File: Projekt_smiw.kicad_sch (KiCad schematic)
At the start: 19 parts, among them J1 PWR 5V, J2 JTAG, J3 Conn, SW1 SW_Omron_B3FS, SW2 SW_Omron_B3FS, U1 NCP1117-2.85_TO252, U2 ESP32-S3-PICO-1

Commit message: Orange 21.39
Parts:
- added J7: PWR 5V, symbol Connector_Generic:Conn_01x02
- C6: value ??? -> 10μF
- R2: value 0 -> 10k
- R6: value ??? -> 10k
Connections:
- net BOOT: now also C2.2, SW2.2; no longer R2.2
- net GND: now also J7.2 (Pin_2)
- net ROW 3: now also U2.19 (GPIO14); no longer U2.8 (GPIO3)
- net VDD3: now also R2.1
- new net: J7.1 (Pin_1), R2.2, U2.8 (GPIO3)
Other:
- moved on the sheet: SW2

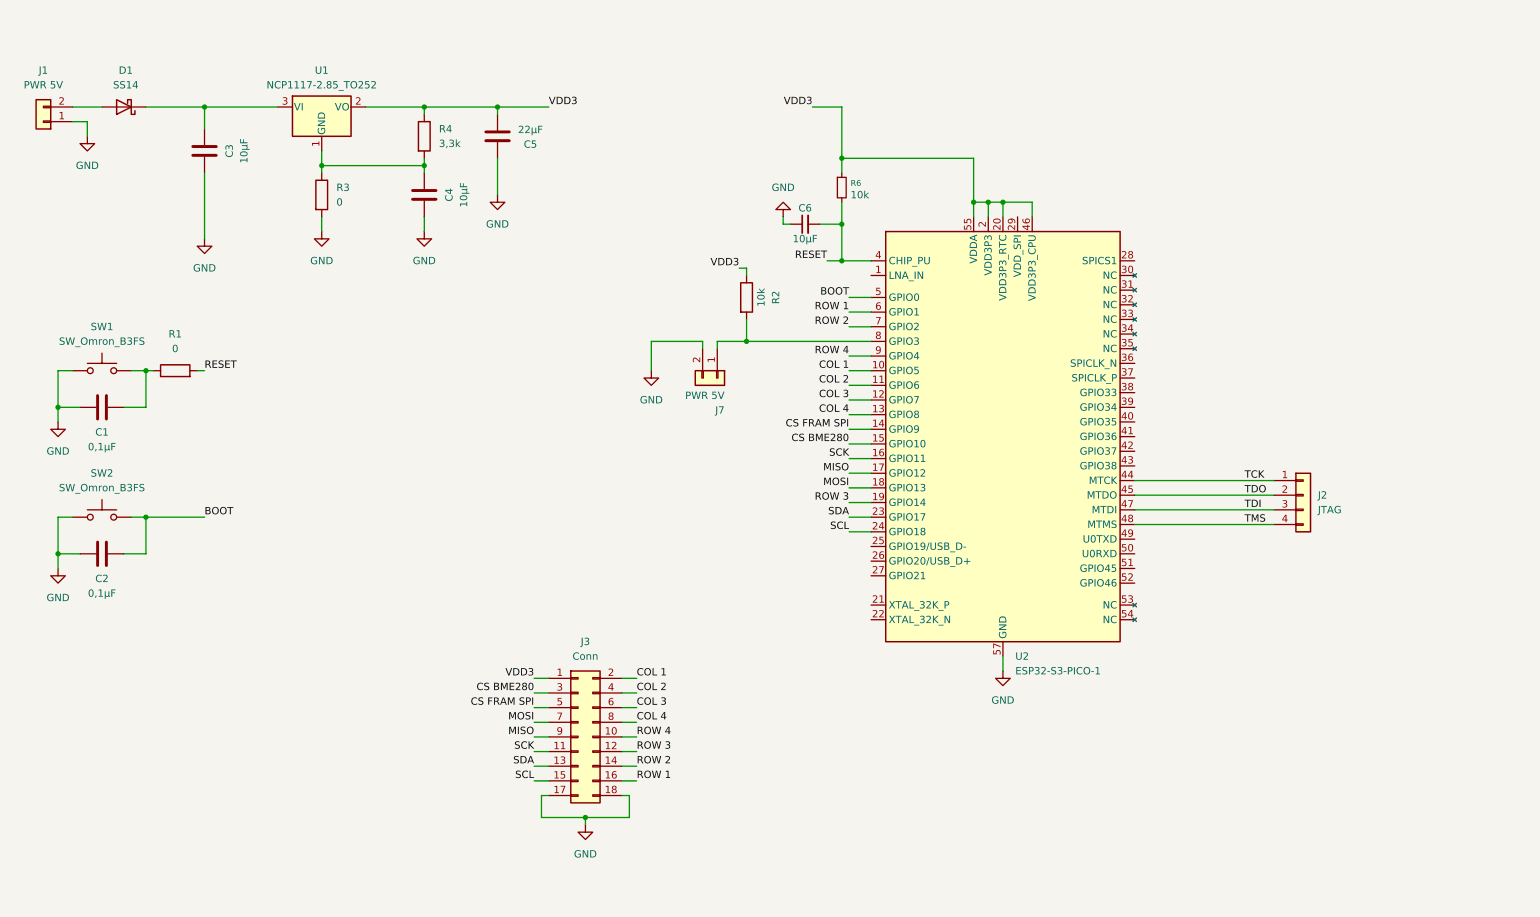
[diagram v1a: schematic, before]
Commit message: USB C update
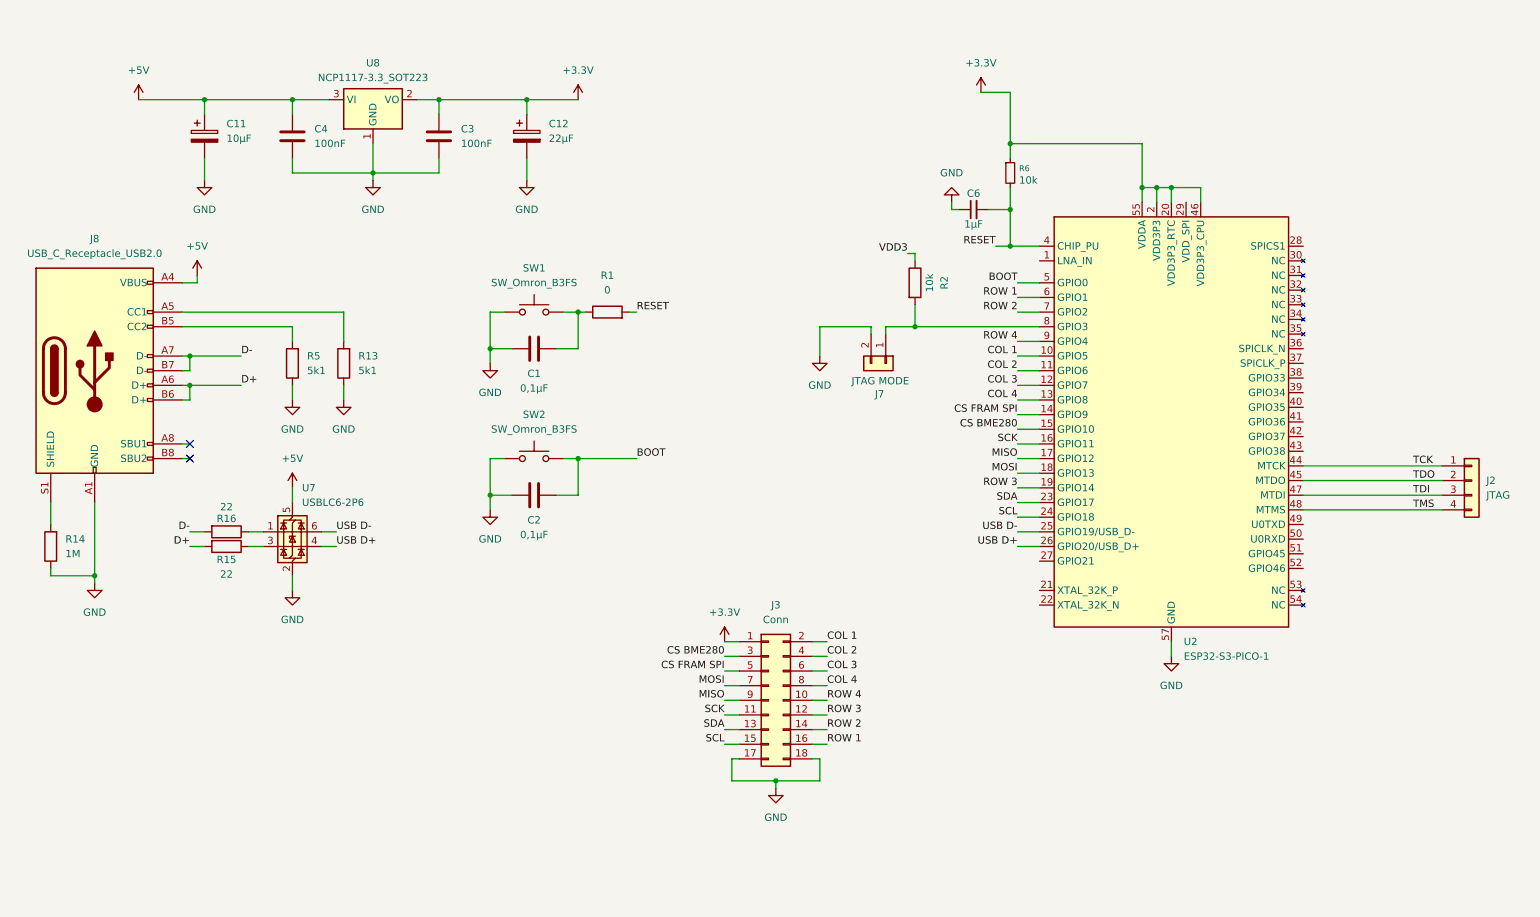
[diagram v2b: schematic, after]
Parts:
- removed C5: 22μF, symbol Device:C
- removed D1: SS14, Diode_SMD:D_SMA, symbol Diode:SS14
- removed J1: PWR 5V, symbol Connector_Generic:Conn_01x02
- removed R3: 0, symbol Device:R
- removed R4: 3,3k, symbol Device:R
- removed U1: NCP1117-2.85_TO252, Package_TO_SOT_SMD:TO-252-2, symbol Regulator_Linear:NCP1117-2.85_TO252
- added C11: 10μF, symbol Device:C_Polarized
- added C12: 22μF, symbol Device:C_Polarized
- added J8: USB_C_Receptacle_USB2.0, symbol Connector:USB_C_Receptacle_USB2.0
- added R13, R5: 5k1, symbol Device:R
- added R14: 1M, symbol Device:R
- added R15, R16: 22, symbol Device:R
- added U7: USBLC6-2P6, Package_TO_SOT_SMD:SOT-666, symbol Power_Protection:USBLC6-2P6
- added U8: NCP1117-3.3_SOT223, Package_TO_SOT_SMD:SOT-223-3_TabPin2, symbol Regulator_Linear:NCP1117-3.3_SOT223
- C3, C4: value 10μF -> 100nF
- C6: value 10μF -> 1μF
- J7: value PWR 5V -> JTAG MODE
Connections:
- net GND: now also C3.2, C4.2, C11.2, C12.2, J8.A1 (GND), J8.A12 (GND), J8.B1 (GND), J8.B12 (GND), R13.1, R14.1, R5.1, U7.2 (GND), U8.1 (GND); no longer C3.1, C4.1
- net VDD3: no longer J3.1 (Pin_1), R6.1, U2.2 (VDD3P3), U2.20 (VDD3P3_RTC), U2.3 (VDD3P3), U2.46 (VDD3P3_CPU), U2.55 (VDDA), U2.56 (VDDA)
- net USB D-: now reaches U2.25 (GPIO19/USB_D-)
- net USB D-: now also U7.6 (I/O1)
- net USB D+: now reaches U2.26 (GPIO20/USB_D+)
- net USB D+: now also U7.4 (I/O2)
- new net: R16.1, U7.1 (I/O1)
- new net: R15.1, U7.3 (I/O2)
- new net: J8.A5 (CC1), R13.2
- new net: J8.B5 (CC2), R5.2
- new net: J8.S1 (SHIELD), R14.2
- new net +3.3V: C12.1, C3.1, J3.1 (Pin_1), R6.1, U2.2 (VDD3P3), U2.20 (VDD3P3_RTC), U2.3 (VDD3P3), U2.46 (VDD3P3_CPU), U2.55 (VDDA), U2.56 (VDDA), U8.2 (VO)
- new net +5V: C11.1, C4.1, J8.A4 (VBUS), J8.A9 (VBUS), J8.B4 (VBUS), J8.B9 (VBUS), U7.5 (VBUS), U8.3 (VI)
- new net D+: J8.A6 (D+), J8.B6 (D+), R15.2
- new net D-: J8.A7 (D-), J8.B7 (D-), R16.2
- no-connect marks 0 -> 2
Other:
- moved on the sheet: C1, C2, C6, J2, J3, J7, R1, R2, R6, SW1, SW2, U2

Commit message: szczerze nie pamiętam co się tutaj zmieniło
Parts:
- removed J7: JTAG MODE, symbol Connector_Generic:Conn_01x02
- removed R14: 1M, symbol Device:R
- removed R15, R16: 22, symbol Device:R
- removed R2: 10k, symbol Device:R
- added R14, R15, R16, R17: 10k, symbol Device:R_Small
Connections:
- net +3.3V: now also R14.1, R15.1, R16.2, R17.2
- net COL 1: now also U2.9 (GPIO4); no longer U2.10 (GPIO5)
- net COL 2: now also U2.10 (GPIO5); no longer U2.11 (GPIO6)
- net COL 3: now also U2.11 (GPIO6); no longer U2.12 (GPIO7)
- net COL 4: now also U2.12 (GPIO7); no longer U2.13 (GPIO8)
- net CS BME280: now also U2.7 (GPIO2), R17.1; no longer U2.15 (GPIO10)
- net CS FRAM SPI: now also U2.6 (GPIO1), R16.1; no longer U2.14 (GPIO9)
- net D+: now also U7.3 (I/O2)
- net D-: now also U7.1 (I/O1)
- net GND: now also J8.S1 (SHIELD)
- net MISO: now also U2.18 (GPIO13); no longer U2.17 (GPIO12)
- net MOSI: now also U2.19 (GPIO14); no longer U2.18 (GPIO13)
- net ROW 1: now also U2.13 (GPIO8); no longer U2.6 (GPIO1)
- net ROW 2: now also U2.14 (GPIO9); no longer U2.7 (GPIO2)
- net ROW 3: now also U2.15 (GPIO10); no longer U2.19 (GPIO14)
- net ROW 4: now also U2.16 (GPIO11); no longer U2.9 (GPIO4)
- net SCK: now also U2.17 (GPIO12); no longer U2.16 (GPIO11)
- net SCL: now also R15.2
- net SDA: now also R14.2
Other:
- note added: "Ja bym wywalił"
- moved on the sheet: C3, U7

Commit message: małe zmiany poprawki dsagolih
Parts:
- removed R16, R17: 10k, symbol Device:R_Small
- renumbered C11 to C1, C4 to C2, C12 to C4, C1 to C5, C2 to C6, C6 to C7, J8 to J1, J3 to J2, J2 to J3, R5 to R1, R13 to R2, R1 to R3, R15 to R4, R14 to R5, U7 to U1, U8 to U2, U2 to U3
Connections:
- no-connect marks 2 -> 21
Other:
- moved on the sheet: C5, C6, J2, R3, SW1, SW2

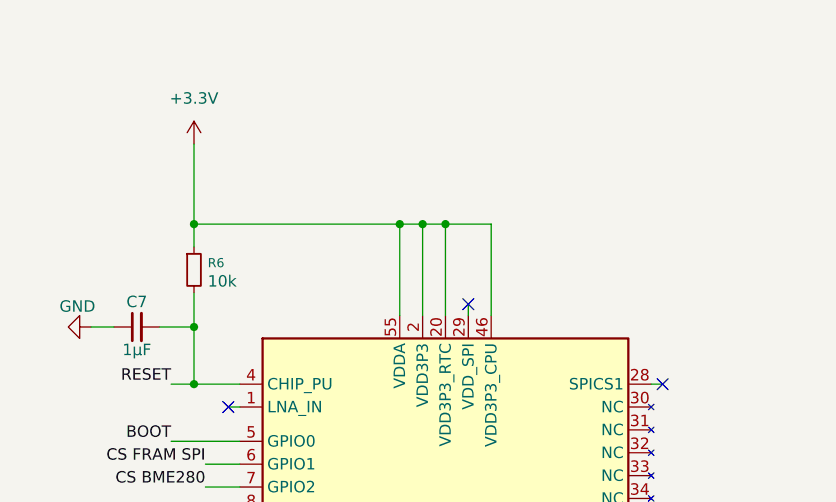
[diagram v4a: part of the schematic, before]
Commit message: dodano kondesnatory 100nF
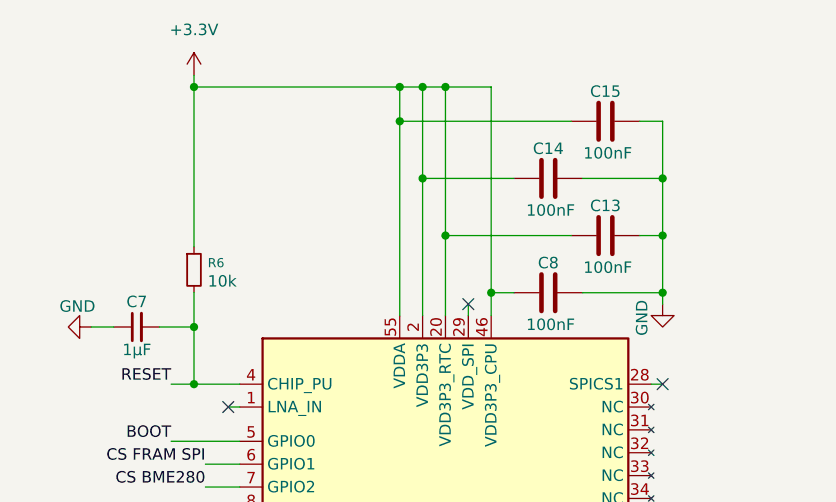
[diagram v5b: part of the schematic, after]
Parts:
- added C13, C14, C15, C8: 100nF, symbol Device:C
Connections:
- net +3.3V: now also C13.1, C14.1, C15.1, C8.1
- net GND: now also C13.2, C14.2, C15.2, C8.2

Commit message: footprinty all, aheoi;rthipoawert;hiogsedho;i yay Halo? Schemat zrobiony ^^ pewnie nie
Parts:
- removed C1: 10μF, symbol Device:C_Polarized
- removed C4: 22μF, symbol Device:C_Polarized
- removed J3: JTAG, symbol Connector_Generic:Conn_01x04
- removed R3: 0, symbol Device:R
- added C16, C4: 10μF, Capacitor_SMD:C_0805_2012Metric, symbol Device:C
- added U8: LM1117DT-3.3, Package_TO_SOT_SMD:TO-252-3_TabPin2, symbol Regulator_Linear:LM1117DT-3.3
- C10: renamed from C15; footprint (none) -> Capacitor_SMD:C_0603_1608Metric
- C11: renamed from C13; footprint (none) -> Capacitor_SMD:C_0603_1608Metric
- C2, C3, C5, C6, C7: footprint (none) -> Capacitor_SMD:C_0603_1608Metric
- C8: renamed from C14; footprint (none) -> Capacitor_SMD:C_0603_1608Metric
- C9: renamed from C8; footprint (none) -> Capacitor_SMD:C_0603_1608Metric
- J1: footprint (none) -> Connector_USB:USB_C_Receptacle_HRO_TYPE-C-31-M-12
- J2: value Conn -> Conn OUT; footprint (none) -> Connector_PinSocket_2.54mm:PinSocket_2x09_P2.54mm_Vertical
- R1, R2: footprint (none) -> Resistor_SMD:R_0603_1608Metric
- R3: renamed from R4; footprint (none) -> Resistor_SMD:R_0603_1608Metric
- R4: renamed from R5; footprint (none) -> Resistor_SMD:R_0603_1608Metric
- R5: renamed from R6; footprint (none) -> Resistor_SMD:R_0603_1608Metric
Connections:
- net +3.3V: now also C4.1
- net +5V: now also C16.1
- net GND: now also J1.SH (SHIELD), C16.2, C4.2; no longer J1.S1 (SHIELD)
- net RESET: now also C5.2, SW1.2
- net ROW 1: now also J2.10 (Pin_10); no longer J2.16 (Pin_16)
- net ROW 2: now also J2.12 (Pin_12); no longer J2.14 (Pin_14)
- net ROW 3: now also J2.14 (Pin_14); no longer J2.12 (Pin_12)
- net ROW 4: now also J2.16 (Pin_16); no longer J2.10 (Pin_10)
- net TCK: no longer names the net of U3.44 (MTCK)
- net TDI: no longer names the net of U3.47 (MTDI)
- net TDO: no longer names the net of U3.45 (MTDO)
- net TMS: no longer names the net of U3.48 (MTMS)
- no-connect marks 21 -> 25
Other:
- note added: "tu były rezystory 0ohm kiedyś"
- note added: "tu były rezystory 22ohm kiedyś"
- note removed: "Ja bym wywalił"

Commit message: awetg
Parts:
- removed J2: Conn OUT, Connector_PinSocket_2.54mm:PinSocket_2x09_P2.54mm_Vertical, symbol Connector_Generic:Conn_02x09_Odd_Even
- added J2: Conn_01x08, Connector_PinSocket_2.54mm:PinSocket_1x08_P2.54mm_Vertical, symbol Connector_Generic:Conn_01x08
- added J3: Conn_01x10, Connector_PinSocket_2.54mm:PinSocket_1x10_P2.54mm_Vertical, symbol Connector_Generic:Conn_01x10
- renumbered C16 to C1, U8 to U3, U3 to U4
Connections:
- net +3.3V: now also J2.1 (Pin_1)
- net COL 1: now also J3.1 (Pin_1)
- net COL 2: now also J3.2 (Pin_2)
- net COL 3: now also J3.3 (Pin_3)
- net COL 4: now also J3.4 (Pin_4)
- net CS BME280: now also J2.2 (Pin_2)
- net CS FRAM SPI: now also J2.3 (Pin_3)
- net GND: now also J3.10 (Pin_10), J3.9 (Pin_9)
- net MISO: now also J2.5 (Pin_5)
- net MOSI: now also J2.4 (Pin_4)
- net ROW 1: now also J3.5 (Pin_5)
- net ROW 2: now also J3.6 (Pin_6)
- net ROW 3: now also J3.7 (Pin_7)
- net ROW 4: now also J3.8 (Pin_8)
- net SCK: now also J2.6 (Pin_6)
- net SCL: now also J2.8 (Pin_8)
- net SDA: now also J2.7 (Pin_7)

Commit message: PCB project procesor
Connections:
- net CS BME280: no longer J2.2 (Pin_2)
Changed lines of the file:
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@@
 	(wire
 		(pts
-			(xy 140.97 137.16) (xy 143.51 137.16)
-		)
-		(stroke
-			(width 0)
-			(type default)
-		)
-	)
-	(wire
-		(pts
 			(xy 240.03 46.99) (xy 240.03 48.26)
 		)
@@
 			"9657c4ae-e888-4b50-8727-5b9f0c124c57" "9e721755-3b25-4e25-9e9e-5b7f326dde6b"
 			"b7078fb9-556c-42cd-9c72-1364b61bb7b2" "bed02eec-c0f3-402a-ba93-5a04d69a145a"
-			"c1143066-96ea-40fb-b9b8-e0da8119856f" "c1f92fc0-29cd-4c20-afaa-2d7abac53f88"
-			"c94cdee4-cb52-4543-aeeb-333f91e50149" "d0665d1e-2d99-400c-8d23-579234d2159c"
-			"d5b7ff1f-5721-46bc-83dc-c01325e06c89" "e0af1000-64cf-4d41-b3e3-b55613b95f97"
-			"eab3a06f-78c8-40ab-9cbd-8287dd0071e0" "f59b5e1a-80af-4df4-b6c4-3f88f4bdf7e3"
+			"c1f92fc0-29cd-4c20-afaa-2d7abac53f88" "c94cdee4-cb52-4543-aeeb-333f91e50149"
+			"d0665d1e-2d99-400c-8d23-579234d2159c" "d5b7ff1f-5721-46bc-83dc-c01325e06c89"
+			"e0af1000-64cf-4d41-b3e3-b55613b95f97" "eab3a06f-78c8-40ab-9cbd-8287dd0071e0"
+			"f59b5e1a-80af-4df4-b6c4-3f88f4bdf7e3"
 		)
 	)
